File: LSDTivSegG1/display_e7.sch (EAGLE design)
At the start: 95 parts, among them IC1 MEGA8-P, IC2 MAX232, IC3 PCF8574P, IC4 PCF8574P, IC5 PCF8574P, IC6 PCF8574P

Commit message: exported the current version of the eagle 7 compatible file for display board
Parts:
- removed R4: 1k0, rcl:R-EU_0207/10
- added C10, C11, C12, C13: 100nF, rcl:C-EU025-025X050
- added JP2: (no value), pinhead:PINHD-2X3
- R2: value 10k -> 5k
- R3: value 2k2 -> 15k
- U$2: value PCB -> DISPLAY_FRAME; device lsd2016:PCB -> lsd2016:DISPLAY_FRAME
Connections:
- new net RS232RX_CON: JP2.3, X1.2
- new net RS232TX_CON: JP2.4, X1.3
- net +5V: now also C10.1, C11.1, C12.1, C13.1, IC2P.VCC; no longer C6.-, R12.2, R13.2, R14.2, R15.2, R16.2, R17.2, R18.2, R19.2, R20.2, R21.2, R22.2, R23.2, R24.2, R25.2, R26.2, R27.2, R28.2, R29.2, R30.2, R31.2, R32.2, R33.2, R34.2, R35.2
- net GND: now also C10.2, C11.2, C12.2, C13.2, C6.-, IC2P.GND, R12.2, R13.2, R14.2, R15.2, R16.2, R17.2, R18.2, R19.2, R20.2, R21.2, R22.2, R23.2, R24.2, R25.2, R26.2, R27.2, R28.2, R29.2, R30.2, R31.2, R32.2, R33.2, R34.2, R35.2; no longer R4.2
- net N$9: no longer R4.1
- net RS232RX: now also JP2.1, JP2.6; no longer X1.4
- net RS232TX: now also JP2.2, JP2.5; no longer X1.3
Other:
- moved on the sheet: C6, C7, R3

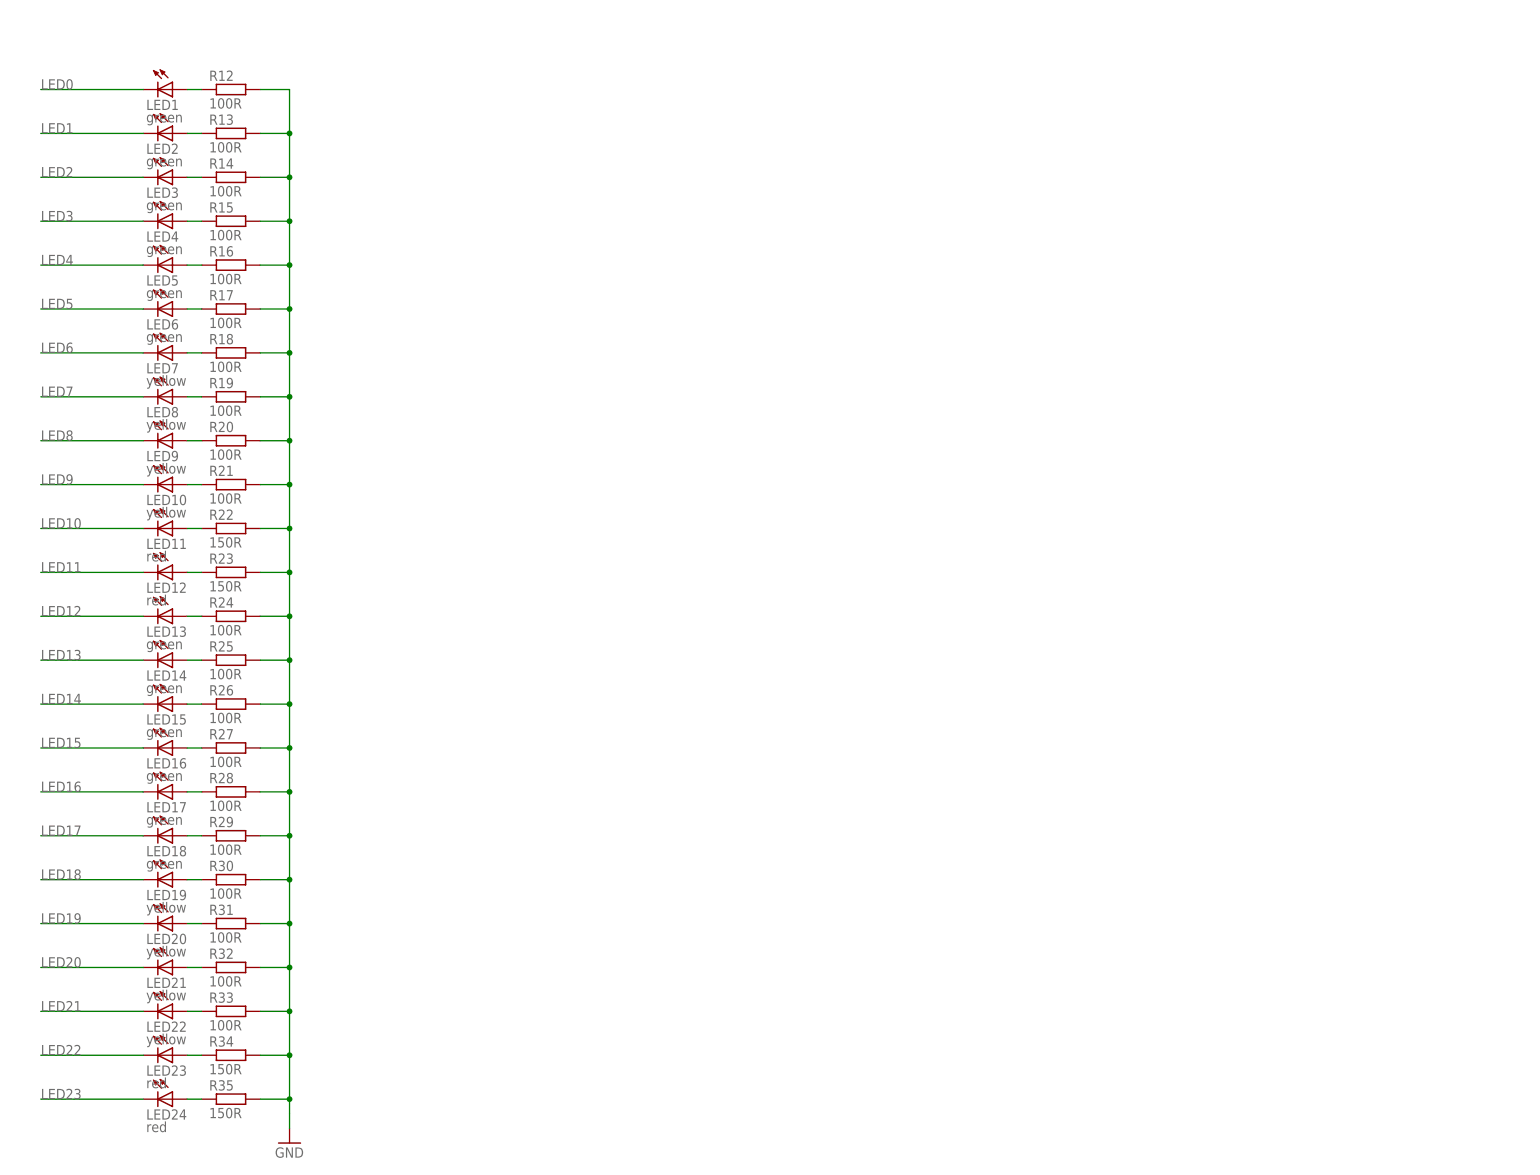
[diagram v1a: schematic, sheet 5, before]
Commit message: updated eagle7 copatible exports of display and leistung boards
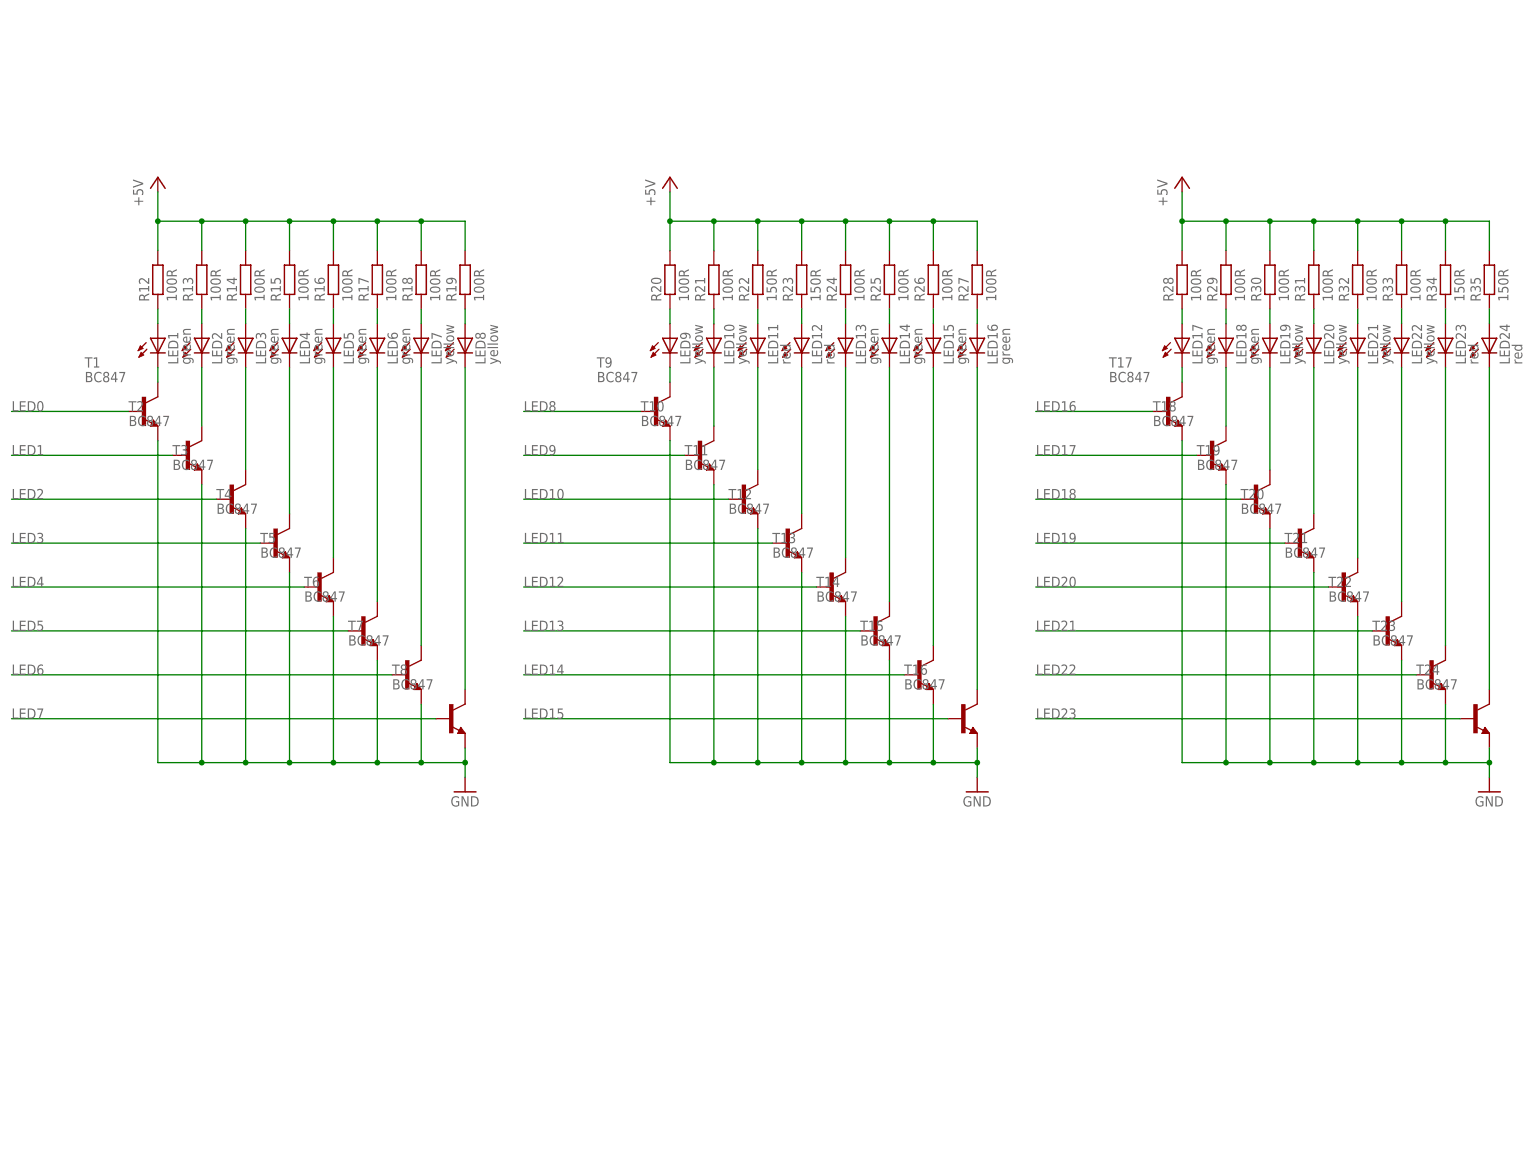
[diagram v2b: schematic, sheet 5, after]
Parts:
- added R4, R40, R41, R42, R43, R44, R45, R46: 10k, rcl:R-EU_R0805
- added T1, T10, T11, T12, T13, T14, T15, T16, T17, T18, T19, T2, T20, T21, T22, T23, T24, T3, T4, T5, T6, T7, T8, T9: BC847, transistor:BC847
- LED17, LED20, LED21, LED22, LED23, LED24: SPICEPREFIX (none) -> L
- LED18: SPICEPREFIX (none) -> X
- LED19: SPICEPREFIX (none) -> B
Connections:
- removed net SDL: IC3.SCL, IC4.SCL, IC5.SCL, IC6.SCL
- new net N$49: R4.1, S8.P
- new net N$50: R41.1, S6.P
- new net N$51: LED9.C, T9.C
- new net N$52: R45.1, S2.P1
- new net N$53: LED1.C, T1.C
- new net N$54: LED2.C, T2.C
- new net N$55: LED3.C, T3.C
- new net N$56: LED4.C, T4.C
- new net N$57: LED5.C, T5.C
- new net N$58: LED6.C, T6.C
- new net N$59: LED17.C, T17.C
- new net N$60: LED10.C, T10.C
- new net N$61: LED11.C, T11.C
- new net N$62: LED12.C, T12.C
- new net N$63: LED13.C, T13.C
- new net N$64: LED14.C, T14.C
- new net N$65: LED7.C, T7.C
- new net N$66: LED8.C, T8.C
- new net N$67: LED15.C, T15.C
- new net N$68: LED16.C, T16.C
- new net N$69: LED18.C, T18.C
- new net N$70: LED19.C, T19.C
- new net N$71: LED20.C, T20.C
- new net N$72: LED21.C, T21.C
- new net N$73: LED22.C, T22.C
- new net N$74: LED23.C, T23.C
- new net N$75: LED24.C, T24.C
- new net N$76: R43.1, S4.P1
- new net N$77: R44.1, S3.P
- new net N$78: R42.1, S5.P1
- new net N$79: R46.1, S1.P
- new net N$80: R40.1, S7.P1
- net +5V: now also R12.2, R13.2, R14.2, R15.2, R16.2, R17.2, R18.2, R19.2, R20.2, R21.2, R22.2, R23.2, R24.2, R25.2, R26.2, R27.2, R28.2, R29.2, R30.2, R31.2, R32.2, R33.2, R34.2, R35.2, R4.2, R40.2, R41.2, R42.2, R43.2, R44.2, R45.2, R46.2
- net BTN0: no longer S8.P
- net BTN1: no longer S7.P1
- net BTN2: no longer S6.P
- net BTN3: no longer S5.P1
- net BTN4: no longer S4.P1
- net BTN5: no longer S3.P
- net BTN6: no longer S2.P1
- net BTN7: no longer S1.P
- net GND: now also T1.E, T10.E, T11.E, T12.E, T13.E, T14.E, T15.E, T16.E, T17.E, T18.E, T19.E, T2.E, T20.E, T21.E, T22.E, T23.E, T24.E, T3.E, T4.E, T5.E, T6.E, T7.E, T8.E, T9.E; no longer R12.2, R13.2, R14.2, R15.2, R16.2, R17.2, R18.2, R19.2, R20.2, R21.2, R22.2, R23.2, R24.2, R25.2, R26.2, R27.2, R28.2, R29.2, R30.2, R31.2, R32.2, R33.2, R34.2, R35.2
- net LED0: now also T1.B; no longer LED1.C
- net LED1: now also T2.B; no longer LED2.C
- net LED10: now also T11.B; no longer LED11.C
- net LED11: now also T12.B; no longer LED12.C
- net LED12: now also T13.B; no longer LED13.C
- net LED13: now also T14.B; no longer LED14.C
- net LED14: now also T15.B; no longer LED15.C
- net LED15: now also T16.B; no longer LED16.C
- net LED16: now also T17.B; no longer LED17.C
- net LED17: now also T18.B; no longer LED18.C
- net LED18: now also T19.B; no longer LED19.C
- net LED19: now also T20.B; no longer LED20.C
- net LED2: now also T3.B; no longer LED3.C
- net LED20: now also T21.B; no longer LED21.C
- net LED21: now also T22.B; no longer LED22.C
- net LED22: now also T23.B; no longer LED23.C
- net LED23: now also T24.B; no longer LED24.C
- net LED3: now also T4.B; no longer LED4.C
- net LED4: now also T5.B; no longer LED5.C
- net LED5: now also T6.B; no longer LED6.C
- net LED6: now also T7.B; no longer LED7.C
- net LED7: now also T8.B; no longer LED8.C
- net LED8: now also T9.B; no longer LED9.C
- net LED9: now also T10.B; no longer LED10.C
- net SCL: now also IC3.SCL, IC4.SCL, IC5.SCL, IC6.SCL
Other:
- moved on the sheet: LED1, LED10, LED11, LED12, LED13, LED14, LED15, LED16, LED17, LED18, LED19, LED2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
